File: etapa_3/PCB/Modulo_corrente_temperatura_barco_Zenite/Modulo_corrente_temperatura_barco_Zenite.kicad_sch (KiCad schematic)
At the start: 46 parts, among them J1 RJ45_Shielded, J2 Conn_01x03, U2 LM7805, U3 TLV9004IDR, U4 MCP2515-xSO, U5 MCP2551-I-SN, Y1 16MHz

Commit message: sallen-key filter fixed to match 0.707 quality factor
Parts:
- C7: value 470p -> 1nF
- R11: value 4k7 -> 10k
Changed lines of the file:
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@@
 			)
 		)
-		(property "Value" "470p"
+		(property "Value" "1nF"
 			(at 247.65 130.81 90)
 			(effects
@@
 			)
 		)
-		(property "Value" "4k7"
+		(property "Value" "10k"
 			(at 227.33 102.87 90)
 			(effects

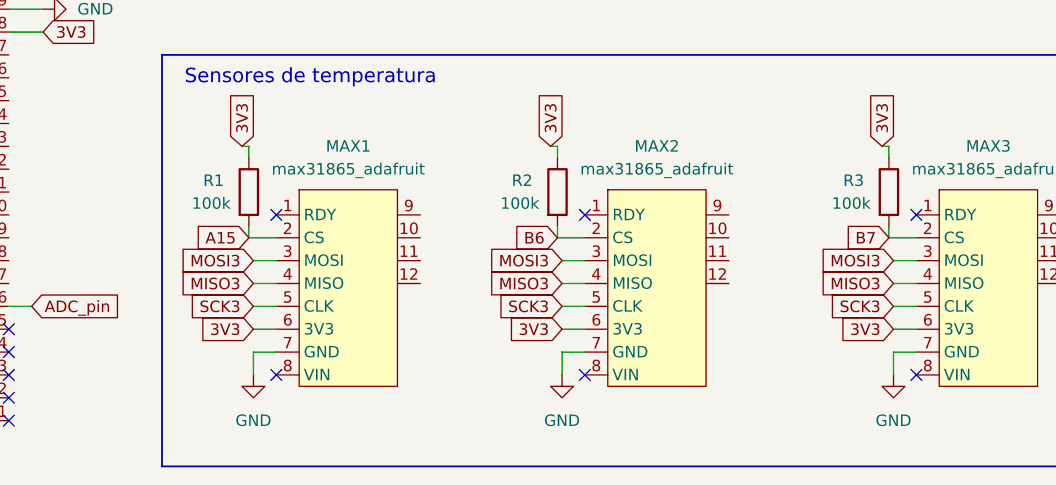
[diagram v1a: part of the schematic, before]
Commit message: MCP2515_driver and code for test added
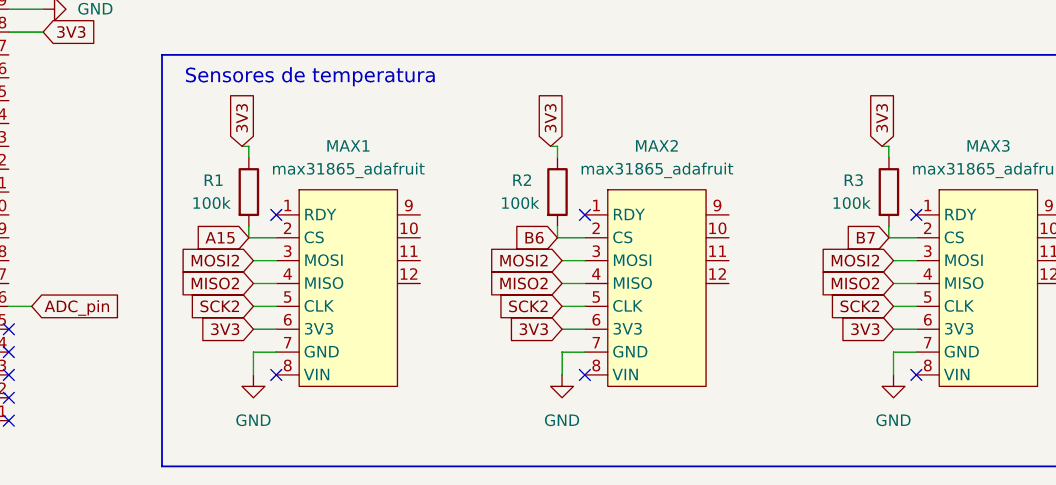
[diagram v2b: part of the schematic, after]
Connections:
- net MISO2: now also MAX1.4 (MISO), MAX2.4 (MISO), MAX3.4 (MISO)
- net MISO3: no longer MAX1.4 (MISO), MAX2.4 (MISO), MAX3.4 (MISO)
- net MOSI2: now also MAX1.3 (MOSI), MAX2.3 (MOSI), MAX3.3 (MOSI)
- net MOSI3: no longer MAX1.3 (MOSI), MAX2.3 (MOSI), MAX3.3 (MOSI)
- net SCK2: now also MAX1.5 (CLK), MAX2.5 (CLK), MAX3.5 (CLK)
- net SCK3: no longer MAX1.5 (CLK), MAX2.5 (CLK), MAX3.5 (CLK)

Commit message: update readme.rst
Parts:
- added J2: RJ45_Shielded, symbol Connector:RJ45_Shielded
- renumbered J2 to J3
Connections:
- net CAN_18V: now also J2.4, J2.5
- net CAN_H: now also J2.1
- net CAN_L: now also J2.2
- net GND: now also J2.3, J2.6, J2.7, J2.8, J2.SH
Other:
- moved on the sheet: C1, C12, C13, C2, C3, C4, D1, D2, D3, D4, D5, F1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

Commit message: PCB layout V1 added - DRC review nedded
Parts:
- removed unit 1 of U3
- added R15: 0R, Resistor_SMD:R_0805_2012Metric_Pad1.20x1.40mm_HandSolder, symbol Device:R
- added unit 2 of U3
- C1, C12, C13: footprint (none) -> Capacitor_THT:CP_Radial_D6.3mm_P2.50mm
- C10, C2, C6, C7, C9: footprint (none) -> Capacitor_SMD:C_0805_2012Metric_Pad1.18x1.45mm_HandSolder
- C11, C3, C4, C5, C8: footprint (none) -> Capacitor_THT:C_Disc_D7.5mm_W2.5mm_P5.00mm
- D1, D2, D3, D4, D5: footprint (none) -> Diode_THT:D_5W_P10.16mm_Horizontal
- F1: footprint (none) -> pi-III-lib:fuse_holder
- J1, J2: footprint (none) -> Connector_RJ:RJ45_Ninigi_GE
- J3: footprint (none) -> pi-III-lib:B3BXHALFSN
- R1, R2, R3: footprint (none) -> Resistor_THT:R_Axial_DIN0207_L6.3mm_D2.5mm_P10.16mm_Horizontal
- R10, R11, R12, R13, R4, R5, R6, R7, R9: footprint (none) -> Resistor_SMD:R_0805_2012Metric_Pad1.20x1.40mm_HandSolder
- R14, R8: footprint (none) -> Resistor_SMD:R_2010_5025Metric_Pad1.40x2.65mm_HandSolder
- U2: footprint Package_TO_SOT_THT:TO-220-3_Vertical -> Package_TO_SOT_THT:TO-220-3_Horizontal_TabDown
- U3: value TLV9004IDR -> TLV9004
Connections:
- net 5V: no longer MIC1.18 (5V)
- net GND: now also R15.2; no longer C5.2, C6.2, R10.2, R14.2, R5.2, R8.2, U3.11 (V-)
- net A8: now reaches MIC1.5 (A8)
- net A8: now also MAX1.2 (CS), R1.2
- net A9: now reaches MIC1.6 (A9)
- net A9: now also MAX2.2 (CS), R2.2
- net A10: now reaches MIC1.7 (A10)
- net A10: now also MAX3.2 (CS), R3.2
- net at R4.2, R5.1: now also U3.5 (+)
- net at R6.2: now also U3.6 (-), U3.7
- removed net A15: MAX1.2 (CS), MIC1.10 (A15), R1.2
- removed net B6: MAX2.2 (CS), MIC1.14 (B6), R2.2
- removed net B7: MAX3.2 (CS), MIC1.15 (B7), R3.2
- new net AGND: C5.2, C6.2, R10.2, R14.2, R15.1, R5.2, R8.2, U3.11 (V-)
- no-connect marks 13 -> 29
